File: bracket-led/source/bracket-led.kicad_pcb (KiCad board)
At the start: 2 copper layers, 27 x 7 mm, 5 parts, among them J1 SM08B-SURS-TF(LF)(SN)

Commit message: production files added (i.e. gerber and dxf)
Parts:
- H1, H2: footprint Open Ephys:SLP3-150-100-R -> Open Ephys:BIVAR_SLP3-150-100-R
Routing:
- net /G2: track 21.7 -> 21.1 mm
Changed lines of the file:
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@@
       (outputformat 1)
       (mirror false)
-      (drillshape 1)
+      (drillshape 0)
       (scaleselection 1)
-      (outputdirectory "")
+      (outputdirectory "../production/")
     )
   )
@@
   (footprint "Open Ephys:JST_SM08B-SURS-TF(LF)(SN)" (layer "F.Cu")
     (at 39.75 51)
-    (descr "JST Connector Vertical Entry 8 pins")
+    (descr "JST Connector Horizontal Entry 8 pins")
     (property "Sheetfile" "bracket-led.kicad_sch")
     (property "Sheetname" "")
@@
     (pad "8" smd roundrect (at 2.8 -1.15) (size 0.5 1) (layers "F.Cu" "F.Paste" "F.Mask") (roundrect_rratio 0.25)
       (net 6 "/B2") (pinfunction "Pin_8") (pintype "passive"))
-    (pad "MP" smd roundrect (at -4.1 0.8) (size 1.2 1.7) (layers "F.Cu" "F.Paste" "F.Mask") (roundrect_rratio 0.208333))
-    (pad "MP" smd roundrect (at 4.1 0.8) (size 1.2 1.7) (layers "F.Cu" "F.Paste" "F.Mask") (roundrect_rratio 0.208333))
-    (model "${OE_3D_DIR}/SM08B-SURS-TF.STEP"
-      (offset (xyz 2.6 4.7 0))
-      (scale (xyz 1 1 1))
-      (rotate (xyz -90 0 0))
+    (pad "MP" smd roundrect (at -4.1 0.8) (size 1.2 1.7) (layers "F.Cu" "F.Paste" "F.Mask") (roundrect_rratio 0.2083333333))
+    (pad "MP" smd roundrect (at 4.1 0.8) (size 1.2 1.7) (layers "F.Cu" "F.Paste" "F.Mask") (roundrect_rratio 0.2083333333))
+    (model "${OE_3D_DIR}/JST_SM08B-SURS-TF.STEP"
+      (offset (xyz 0 0 0))
+      (scale (xyz 1 1 1))
+      (rotate (xyz 0 0 0))
     )
   )
@@
     )
   )
-  (footprint "Open Ephys:SLP3-150-100-R" (layer "F.Cu")
+  (footprint "Open Ephys:BIVAR_SLP3-150-100-R" (layer "F.Cu")
     (at 52.5 52.69176 180)
     (property "Sheetfile" "bracket-led.kicad_sch")
@@
     (property "ki_description" "Compact Light Pipe")
     (attr smd)
-    (fp_text reference "H2" (at -3.5 -1.0315 unlocked) (layer "F.SilkS")
-        (effects (font (size 1 1) (thickness 0.1)))
-    )
-    (fp_text value "SLP3-150-100-R" (at 0 -0.0315 180 unlocked) (layer "F.Fab")
+    (fp_text reference "H2" (at -3.5 -1.05824 unlocked) (layer "F.SilkS")
+        (effects (font (size 1 1) (thickness 0.1)))
+    )
+    (fp_text value "SLP3-150-100-R" (at 0 6.096 180 unlocked) (layer "F.Fab")
         (effects (font (size 1 1) (thickness 0.15)))
     )
@@
     (pad "" np_thru_hole circle (at -1.27 0 180) (size 1.1684 1.1684) (drill 1.1684) (layers "F&B.Cu" "*.Mask"))
     (pad "" np_thru_hole circle (at 1.27 0 180) (size 1.1684 1.1684) (drill 1.1684) (layers "F&B.Cu" "*.Mask"))
-    (model "${OE_3D_DIR}/BIVAR__INC_SLP3-150-100-R.STEP"
-      (offset (xyz 0 0 0))
-      (scale (xyz 1 1 1))
-      (rotate (xyz -90 0 90))
-    )
-  )
-  (footprint "Open Ephys:SLP3-150-100-R" (layer "F.Cu")
+    (model "${OE_3D_DIR}/BIVAR_SLP3-150-100-R.STEP"
+      (offset (xyz 0 0 0))
+      (scale (xyz 1 1 1))
+      (rotate (xyz -0 0 0))
+    )
+  )
+  (footprint "Open Ephys:BIVAR_SLP3-150-100-R" (layer "F.Cu")
     (at 47.5 52.69176 180)
     (property "Sheetfile" "bracket-led.kicad_sch")
@@
     (property "ki_description" "Compact Light Pipe")
     (attr smd)
-    (fp_text reference "H1" (at 3.5 -1.0315 unlocked) (layer "F.SilkS")
-        (effects (font (size 1 1) (thickness 0.1)))
-    )
-    (fp_text value "SLP3-150-100-R" (at 0 -0.0315 180 unlocked) (layer "F.Fab")
+    (fp_text reference "H1" (at 3.5 -1.05824 unlocked) (layer "F.SilkS")
+        (effects (font (size 1 1) (thickness 0.1)))
+    )
+    (fp_text value "SLP3-150-100-R" (at 0 6.096 180 unlocked) (layer "F.Fab")
         (effects (font (size 1 1) (thickness 0.15)))
     )
@@
     (pad "" np_thru_hole circle (at -1.27 0 180) (size 1.1684 1.1684) (drill 1.1684) (layers "F&B.Cu" "*.Mask"))
     (pad "" np_thru_hole circle (at 1.27 0 180) (size 1.1684 1.1684) (drill 1.1684) (layers "F&B.Cu" "*.Mask"))
-    (model "${OE_3D_DIR}/BIVAR__INC_SLP3-150-100-R.STEP"
-      (offset (xyz 0 0 0))
-      (scale (xyz 1 1 1))
-      (rotate (xyz -90 0 90))
+    (model "${OE_3D_DIR}/BIVAR_SLP3-150-100-R.STEP"
+      (offset (xyz 0 0 0))
+      (scale (xyz 1 1 1))
+      (rotate (xyz -0 0 0))
     )
   )
@@
   (gr_line (start 32.75 49.73476) (end 31.5 49.73476)
     (stroke (width 0.1) (type default)) (layer "Edge.Cuts"))
-  (gr_text "Rev. A" (at 34.5 54.25) (layer "F.Mask")
+  (gr_text "Rev. A" (at 33 54.25) (layer "F.Mask")
     (effects (font (size 0.5 0.5) (thickness 0.125)) (justify left bottom))
   )
@@
   (segment (start 49 49.25) (end 49.25 49) (width 0.25) (layer "B.Cu") (net 3))
   (segment (start 40.1 49.25) (end 49 49.25) (width 0.25) (layer "B.Cu") (net 3))
-  (segment (start 41.85 54.25) (end 53.568274 54.25) (width 0.25) (layer "F.Cu") (net 4))
+  (segment (start 41.35 53.75) (end 54.068274 53.75) (width 0.25) (layer "F.Cu") (net 4))
+  (segment (start 54.068274 53.75) (end 54.7292 53.089074) (width 0.25) (layer "F.Cu") (net 4))
+  (segment (start 54.7292 53.089074) (end 54.7292 52.2792) (width 0.25) (layer "F.Cu") (net 4))
+  (segment (start 54.7292 52.2792) (end 53.175 50.725) (width 0.25) (layer "F.Cu") (net 4))
   (segment (start 40.15 49.85) (end 40.15 52.55) (width 0.25) (layer "F.Cu") (net 4))
-  (segment (start 54.7292 51.9292) (end 53.525 50.725) (width 0.25) (layer "F.Cu") (net 4))
-  (segment (start 53.568274 54.25) (end 54.7292 53.089074) (width 0.25) (layer "F.Cu") (net 4))
-  (segment (start 54.7292 53.089074) (end 54.7292 51.9292) (width 0.25) (layer "F.Cu") (net 4))
-  (segment (start 53.525 50.725) (end 53.175 50.725) (width 0.25) (layer "F.Cu") (net 4))
-  (segment (start 40.15 52.55) (end 41.85 54.25) (width 0.25) (layer "F.Cu") (net 4))
+  (segment (start 40.15 52.55) (end 41.35 53.75) (width 0.25) (layer "F.Cu") (net 4))
   (segment (start 41.75 49.85) (end 41.75 52.95) (width 0.25) (layer "F.Cu") (net 5))
   (segment (start 54.25 50) (end 53.25 50) (width 0.25) (layer "F.Cu") (net 5))

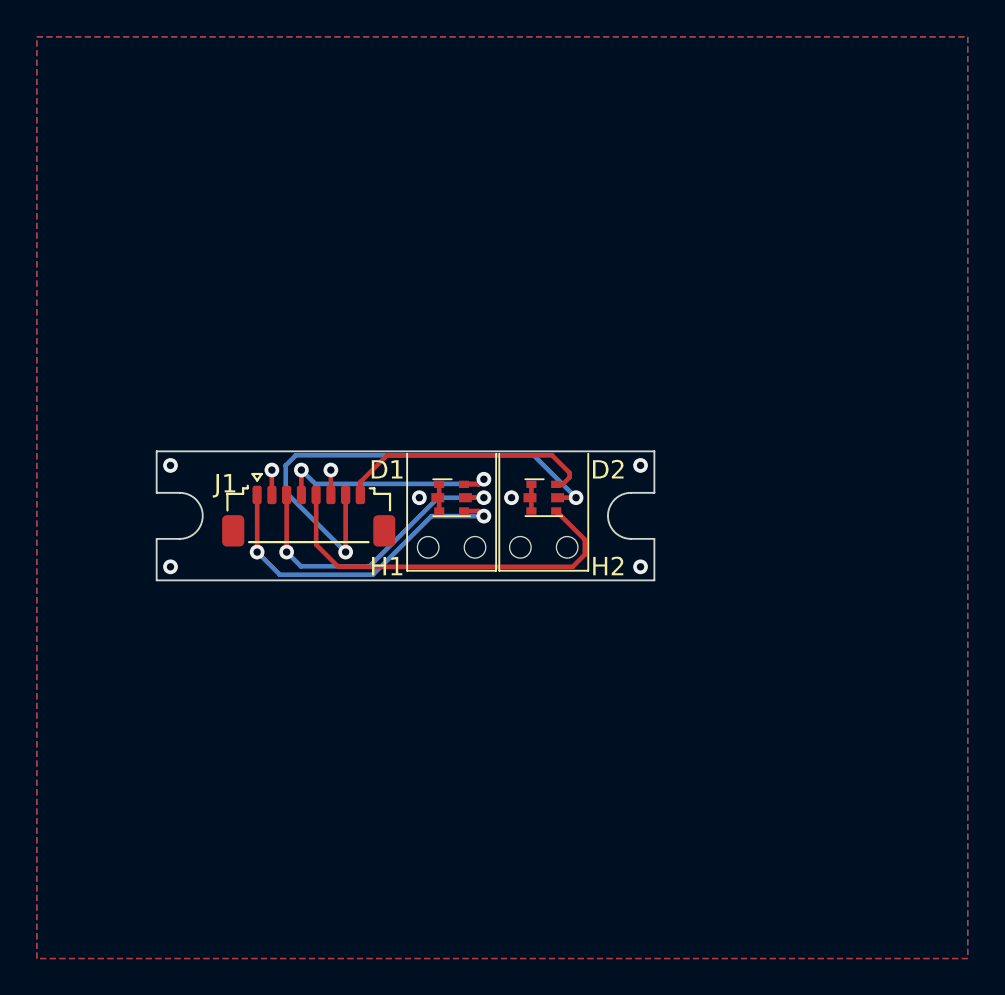
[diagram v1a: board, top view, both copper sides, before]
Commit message: gerbers and kicad ready for review
gerber, bom, pnp files are in production folder for pcb fabrication and assembly. not sure if v-cut will be recognized by jlc. also, the individual pcbs are larger now with LEDs centered
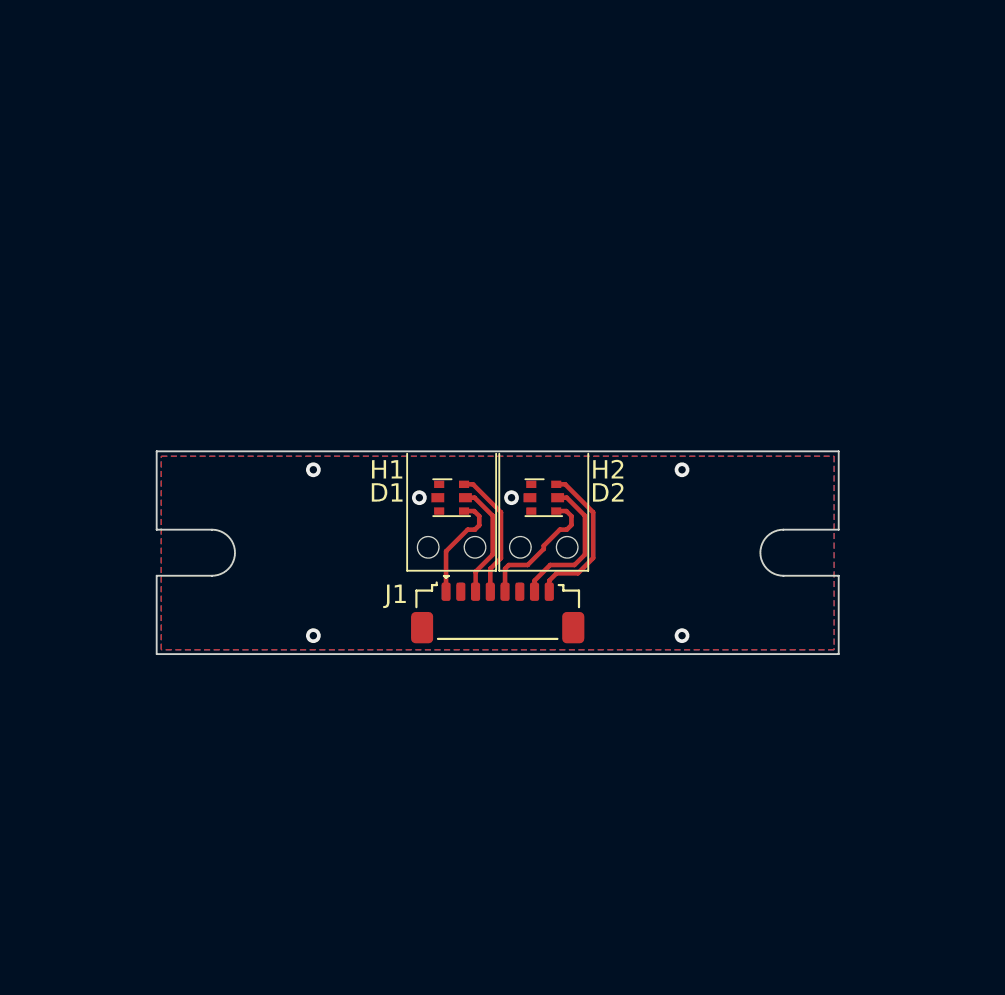
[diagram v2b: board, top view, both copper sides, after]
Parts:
- moved J1 11.5 mm to (50.0, 56.2)
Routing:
- net /R2: track 27.1 -> 8.16 mm, vias 2 -> 0
- net /G2: track 21.1 -> 7.60 mm
- net /G1: track 18.4 -> 6.27 mm, vias 2 -> 0
- net /R1: track 16.7 -> 6.64 mm, vias 2 -> 0
- net GND: track 5.60 -> 0.00 mm, vias 8 -> 6
- net /B1: track 12.9 -> 7.43 mm, vias 2 -> 0
- net /B2: track 14.2 -> 8.85 mm
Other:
- board size 27 x 7 mm -> 37 x 11 mm
